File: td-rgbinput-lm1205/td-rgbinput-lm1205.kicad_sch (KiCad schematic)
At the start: 10 parts, among them J16 Conn_01x06_Male, J2 Conn_01x07_Male, J3 Conn_01x05_Pin, U1 AP2204K-3.3

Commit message: update lm1205 to v1.0
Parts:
- J2: footprint Connector_JST:JST_XH_B7B-XH-AM_1x07_P2.50mm_Vertical -> Connector_JST:JST_XH_B7B-XH-A_1x07_P2.50mm_Vertical
- J3: Digikey (none) -> B5B-XH-A
- U1: value AP2204K-3.3 -> AP2205-33W5-7; Digikey (none) -> 31-AP2205-33W5-7CT-ND
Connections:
- net vga_blue renamed b_yoke
- net vga_green renamed g_yoke
- net vga_red renamed r_yoke
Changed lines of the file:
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@@
   (junction (at 129.54 228.6) (diameter 0) (color 0 0 0 0)
   )
+  (junction (at 140.97 228.6) (diameter 0) (color 0 0 0 0)
+  )
   (junction (at 114.3 215.9) (diameter 0) (color 0 0 0 0)
   )
@@
   )
   (junction (at 322.58 229.87) (diameter 0) (color 0 0 0 0)
+  )
+  (wire (pts (xy 140.97 228.6) (xy 148.59 228.6))
+    (stroke (width 0) (type default))
   )
   (wire (pts (xy 114.3 215.9) (xy 121.92 215.9))
@@
     (stroke (width 0) (type default))
   )
-  (wire (pts (xy 129.54 228.6) (xy 148.59 228.6))
+  (wire (pts (xy 129.54 228.6) (xy 140.97 228.6))
     (stroke (width 0) (type default))
   )
@@
     (effects (font (size 1.27 1.27)) (justify left bottom))
   )
-  (label "vga_vsync" (at 260.35 248.92 0) (fields_autoplaced)
-    (effects (font (size 1.27 1.27)) (justify left bottom))
-  )
   (label "vga_vsync" (at 245.11 200.66 0) (fields_autoplaced)
     (effects (font (size 1.27 1.27)) (justify left bottom))
   )
-  (label "vga_green" (at 260.35 238.76 0) (fields_autoplaced)
-    (effects (font (size 1.27 1.27)) (justify left bottom))
-  )
-  (label "vga_red" (at 260.35 236.22 0) (fields_autoplaced)
-    (effects (font (size 1.27 1.27)) (justify left bottom))
-  )
-  (label "vga_hsync" (at 260.35 246.38 0) (fields_autoplaced)
-    (effects (font (size 1.27 1.27)) (justify left bottom))
-  )
-  (label "vga_blue" (at 260.35 241.3 0) (fields_autoplaced)
-    (effects (font (size 1.27 1.27)) (justify left bottom))
+  (global_label "b_yoke" (shape input) (at 260.35 241.3 0) (fields_autoplaced)
+    (effects (font (size 1.27 1.27)) (justify left))
+    (property "Intersheetrefs" "${INTERSHEET_REFS}" (at 269.0309 241.3 0)
+      (effects (font (size 1.27 1.27)) (justify left) hide)
+    )
   )
   (global_label "GAIN_LOAD" (shape input) (at 148.59 130.81 180) (fields_autoplaced)
@@
     )
   )
+  (global_label "g_yoke" (shape input) (at 260.35 238.76 0) (fields_autoplaced)
+    (effects (font (size 1.27 1.27)) (justify left))
+    (property "Intersheetrefs" "${INTERSHEET_REFS}" (at 269.0309 238.76 0)
+      (effects (font (size 1.27 1.27)) (justify left) hide)
+    )
+  )
+  (global_label "vga_vsync" (shape input) (at 260.35 248.92 0) (fields_autoplaced)
+    (effects (font (size 1.27 1.27)) (justify left))
+    (property "Intersheetrefs" "${INTERSHEET_REFS}" (at 272.1151 248.92 0)
+      (effects (font (size 1.27 1.27)) (justify left) hide)
+    )
+  )
   (global_label "SEP_OE" (shape input) (at 245.11 205.74 0) (fields_autoplaced)
     (effects (font (size 1.27 1.27)) (justify left))
@@
     )
   )
+  (global_label "r_yoke" (shape input) (at 260.35 236.22 0) (fields_autoplaced)
+    (effects (font (size 1.27 1.27)) (justify left))
+    (property "Intersheetrefs" "${INTERSHEET_REFS}" (at 268.6681 236.22 0)
+      (effects (font (size 1.27 1.27)) (justify left) hide)
+    )
+  )
   (global_label "SEP_VSYNC" (shape input) (at 245.11 208.28 0) (fields_autoplaced)
     (effects (font (size 1.27 1.27)) (justify left))
     (property "Intersheetrefs" "${INTERSHEET_REFS}" (at 257.9449 208.28 0)
+      (effects (font (size 1.27 1.27)) (justify left) hide)
+    )
+  )
+  (global_label "vga_hsync" (shape input) (at 260.35 246.38 0) (fields_autoplaced)
+    (effects (font (size 1.27 1.27)) (justify left))
+    (property "Intersheetrefs" "${INTERSHEET_REFS}" (at 272.2965 246.38 0)
       (effects (font (size 1.27 1.27)) (justify left) hide)
     )
@@
       (effects (font (size 1.27 1.27)))
     )
-    (property "Footprint" "Connector_JST:JST_XH_B7B-XH-AM_1x07_P2.50mm_Vertical" (at 240.03 203.2 0)
+    (property "Footprint" "Connector_JST:JST_XH_B7B-XH-A_1x07_P2.50mm_Vertical" (at 240.03 203.2 0)
       (effects (font (size 1.27 1.27)) hide)
     )
@@
       (effects (font (size 1.27 1.27)) hide)
     )
+    (property "Digikey" "B5B-XH-A" (at 153.67 128.27 0)
+      (effects (font (size 1.27 1.27)) hide)
+    )
     (pin "1")
     (pin "2")
@@
       (effects (font (size 1.27 1.27)))
     )
-    (property "Value" "AP2204K-3.3" (at 129.54 212.725 0)
+    (property "Value" "AP2205-33W5-7" (at 129.54 212.725 0)
       (effects (font (size 1.27 1.27)) (justify left))
     )
@@
     )
     (property "Datasheet" "https://www.diodes.com/assets/Datasheets/AP2204.pdf" (at 129.54 215.9 0)
+      (effects (font (size 1.27 1.27)) hide)
+    )
+    (property "Digikey" "31-AP2205-33W5-7CT-ND" (at 129.54 218.44 0)
       (effects (font (size 1.27 1.27)) hide)
     )
@@
     )
   )
-  (symbol (lib_name "GND_1") (lib_id "power:GND") (at 148.59 133.35 270) (unit 1)
+  (symbol (lib_id "power:GND") (at 148.59 133.35 270) (unit 1)
     (in_bom yes) (on_board yes) (dnp no) (fields_autoplaced)
     (property "Reference" "#PWR06" (at 142.24 133.35 0)
@@
         )
       )
+    )
+  )
+  (symbol (lib_id "power:PWR_FLAG") (at 140.97 228.6 0) (unit 1)
+    (in_bom yes) (on_board yes) (dnp no) (fields_autoplaced)
+    (property "Reference" "#FLG01" (at 140.97 226.695 0)
+      (effects (font (size 1.27 1.27)) hide)
+    )
+    (property "Value" "PWR_FLAG" (at 140.97 224.4669 0)
+      (effects (font (size 1.27 1.27)))
+    )
+    (property "Footprint" "" (at 140.97 228.6 0)
+      (effects (font (size 1.27 1.27)) hide)
+    )
+    (property "Datasheet" "~" (at 140.97 228.6 0)
+      (effects (font (size 1.27 1.27)) hide)
+    )
+    (pin "1")
+    (instances
+      (project "td-rgbinput-lm1205"
+        (path "/3efa2ece-8f3f-4a8c-96e9-6ab3ec6f1f70"
+          (reference "#FLG01") (unit 1)
+        )
+      )

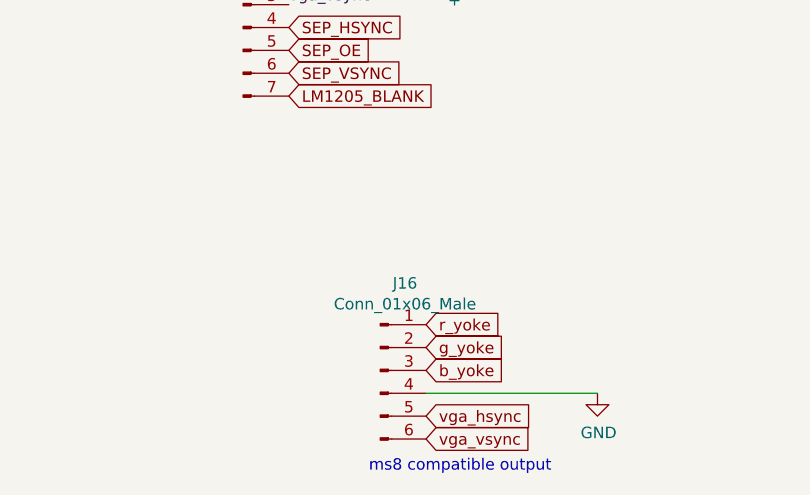
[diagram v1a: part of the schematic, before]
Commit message: remove bad digikey pn
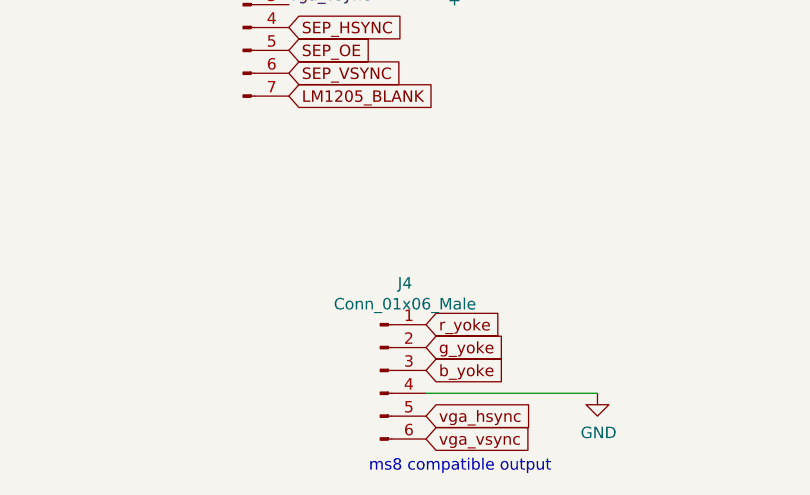
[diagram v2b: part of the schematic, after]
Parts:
- renumbered J16 to J4
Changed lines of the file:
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@@
   (symbol (lib_id "Connector:Conn_01x06_Male") (at 255.27 241.3 0) (unit 1)
     (in_bom yes) (on_board yes) (dnp no)
-    (property "Reference" "J16" (at 258.0132 231.6226 0)
+    (property "Reference" "J4" (at 258.0132 231.6226 0)
       (effects (font (size 1.27 1.27)))
     )
@@
     (instances
       (project "td-rgbinput-lm1205"
-        (path "/3efa2ece-8f3f-4a8c-96e9-6ab3ec6f1f70/c0c68376-68d5-425c-a89c-9d0339373cf7"
-          (reference "J16") (unit 1)
-        )
         (path "/3efa2ece-8f3f-4a8c-96e9-6ab3ec6f1f70"
           (reference "J4") (unit 1)
@@
   (symbol (lib_id "power:GND") (at 279.4 243.84 0) (unit 1)
     (in_bom yes) (on_board yes) (dnp no)
-    (property "Reference" "#PWR0180" (at 279.4 250.19 0)
+    (property "Reference" "#PWR05" (at 279.4 250.19 0)
       (effects (font (size 1.27 1.27)) hide)
     )
@@
     (instances
       (project "td-rgbinput-lm1205"
-        (path "/3efa2ece-8f3f-4a8c-96e9-6ab3ec6f1f70/c0c68376-68d5-425c-a89c-9d0339373cf7"
-          (reference "#PWR0180") (unit 1)
-        )
         (path "/3efa2ece-8f3f-4a8c-96e9-6ab3ec6f1f70"
           (reference "#PWR05") (unit 1)
